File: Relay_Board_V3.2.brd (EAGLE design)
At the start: 140 x 100 mm, 59 parts

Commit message: Board Complete for 2017
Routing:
- net MOTOR_POS: track 0.00 -> 6.09 mm, vias 0 -> 1
- net MOTOR_C_SENSOR: track 23.1 -> 28.6 mm, vias 1 -> 2
- net CAP_SENSOR: track 42.9 -> 47.0 mm, vias 1 -> 2
- net FC_POS: track 52.0 -> 55.1 mm, vias 1 -> 2
- net FC.12: track 119.5 -> 120.5 mm
- net ISO_GND: track 250.2 -> 250.9 mm
- net N$3: track 59.0 -> 59.7 mm

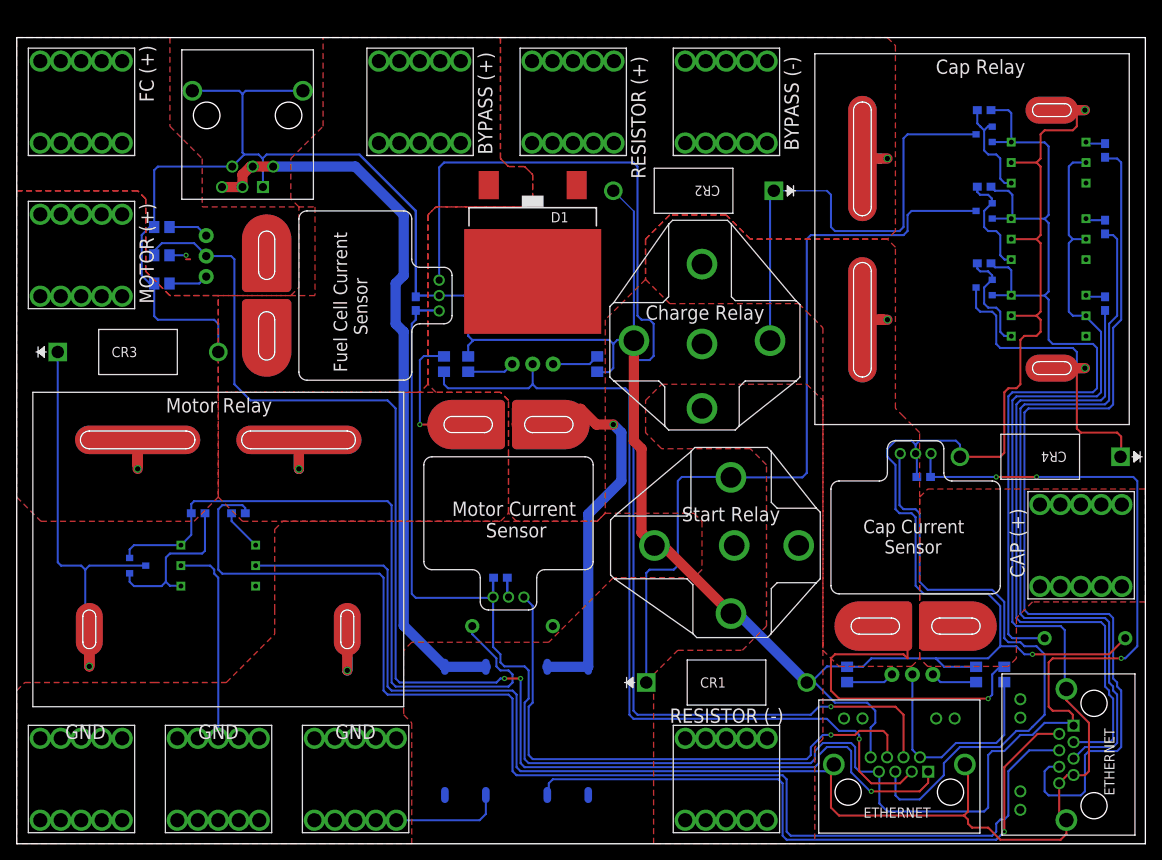
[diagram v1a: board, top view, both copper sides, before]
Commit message: Updated OptoIsolator Part so it is same as FCC
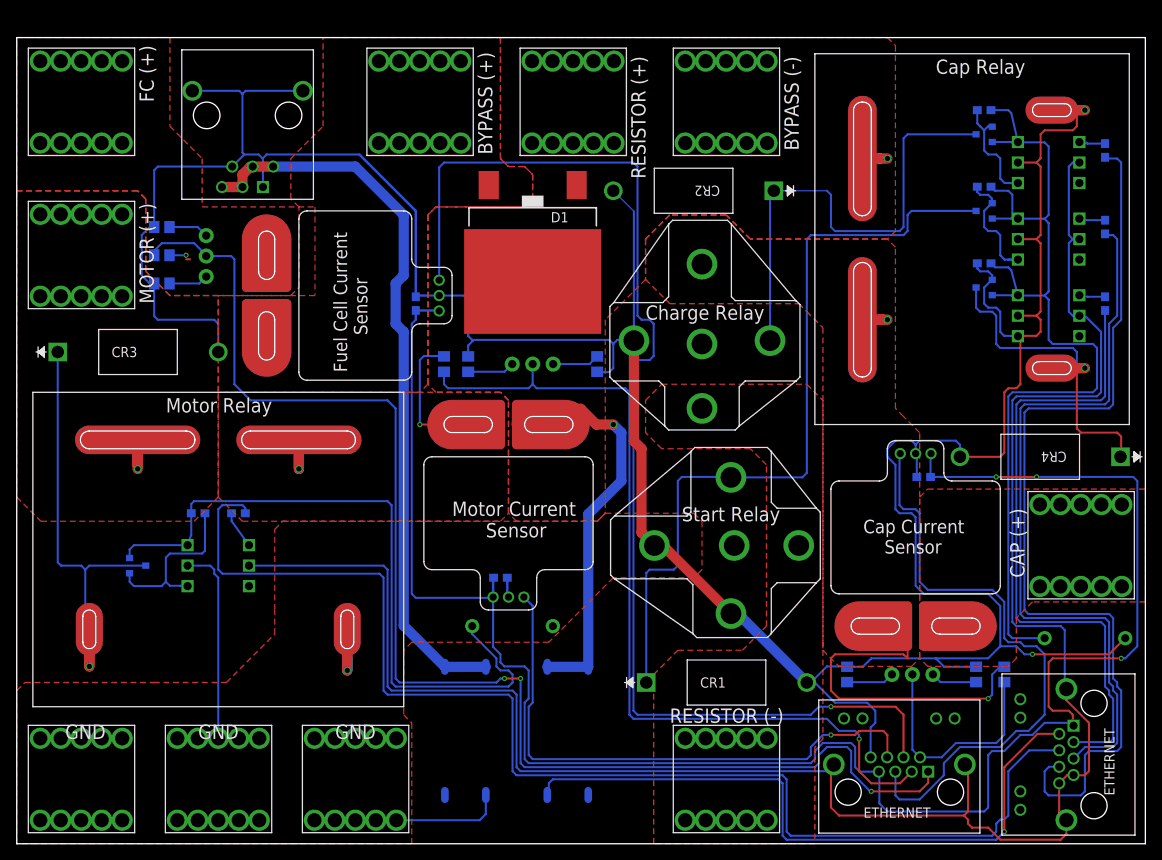
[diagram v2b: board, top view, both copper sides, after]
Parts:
- R14, R15, R16, R2, R4, R5, R6, R7, R8: device Resistor:R0805 -> resistor:R0805
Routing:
- net FC.12: track 120.5 -> 125.2 mm
- net GND: track 447.1 -> 443.8 mm
- net N$21: track 13.7 -> 15.3 mm
- net N$2: track 2.50 -> 4.07 mm
- net ISO_GND: track 250.9 -> 250.0 mm
- net N$1: track 13.2 -> 14.0 mm
- net N$4: track 20.9 -> 21.7 mm
- net N$7: track 13.5 -> 14.3 mm
- net N$8: track 2.44 -> 3.21 mm
- net N$23: track 2.44 -> 3.21 mm
- net N$5: track 5.20 -> 4.66 mm

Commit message: Added Labels to Ethernet connectors
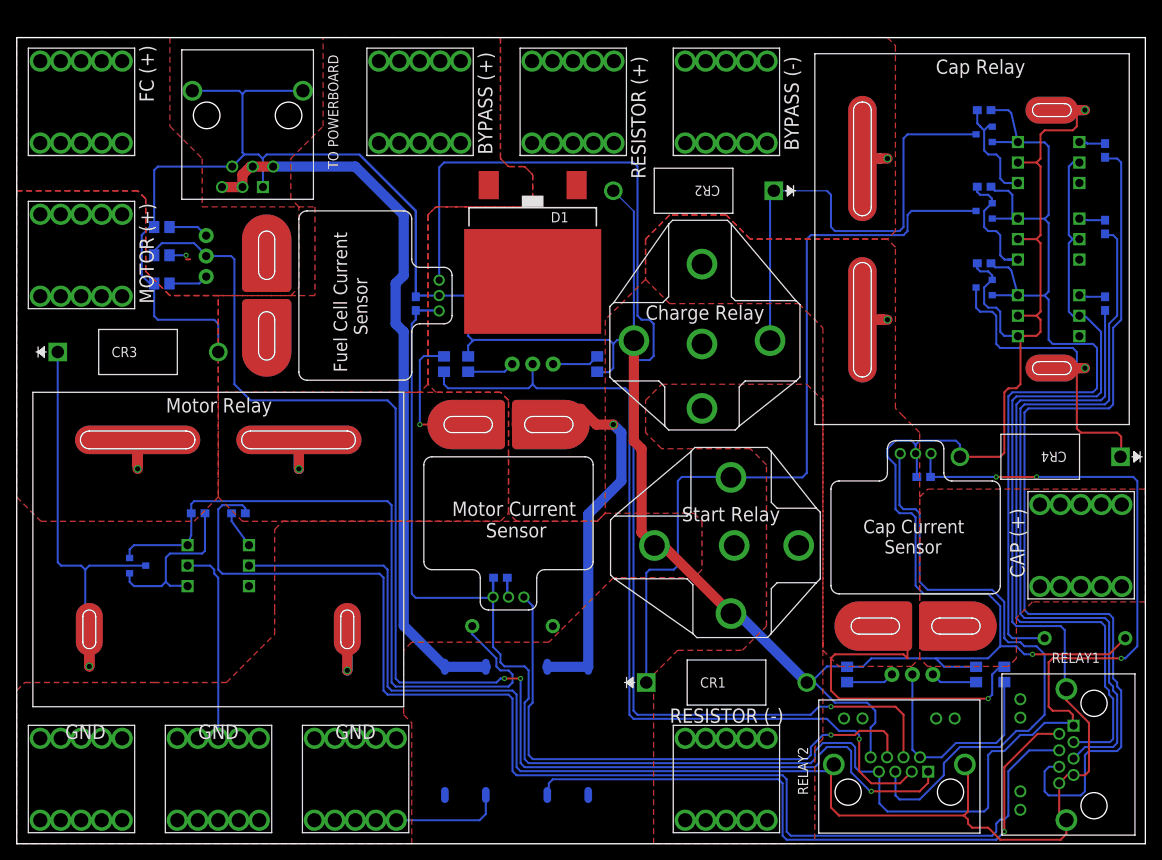
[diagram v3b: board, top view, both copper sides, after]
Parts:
- U$19: value 5555140-6 -> TO POWERBOARD
- renumbered FCC_1 to RELAY1, FCC_2 to RELAY2
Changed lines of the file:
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@@
 </autorouter>
 <elements>
-<element name="FCC_1" library="ETHERNET-3" package="A122645-ND" value="ETHERNET" x="133.630875" y="11.070175" smashed="yes" rot="R90">
-<attribute name="VALUE" x="136.170875" y="5.990175" size="1.27" layer="21" rot="R90"/>
-</element>
-<element name="FCC_2" library="ETHERNET-3" package="A122645-ND" value="ETHERNET" x="109.47946875" y="6.40385" smashed="yes">
-<attribute name="VALUE" x="105.03446875" y="3.22885" size="1.27" layer="21"/>
+<element name="RELAY1" library="ETHERNET-3" package="A122645-ND" value="ETHERNET" x="133.630875" y="11.070175" smashed="yes" rot="R90">
+<attribute name="NAME" x="134.359825" y="23.700875" size="1.27" layer="21" rot="R180"/>
+</element>
+<element name="RELAY2" library="ETHERNET-3" package="A122645-ND" value="ETHERNET" x="109.47946875" y="6.40385" smashed="yes">
+<attribute name="NAME" x="98.16615" y="6.04946875" size="1.27" layer="21" rot="R90"/>
 </element>
 <element name="R4" library="resistor" library_urn="urn:adsk.eagle:library:348" package="R0805" package3d_urn="urn:adsk.eagle:package:26059/1" value="775 (0.1%)" x="103" y="21" smashed="yes" rot="MR90">
@@
 <element name="MOTOR.GROUND" library="Connector 732-3204" package="732-3204-ND" value="732-3204-ND_CONNECTOR" x="25" y="8"/>
 <element name="CAP.GND" library="Connector 732-3204" package="732-3204-ND" value="732-3204-ND_CONNECTOR" x="8" y="8"/>
-<element name="U$19" library="5555140-6 RJ11" package="1734723-1_RJ11" value="5555140-6" x="28" y="84" smashed="yes" rot="R180"/>
+<element name="U$19" library="5555140-6 RJ11" package="1734723-1_RJ11" value="TO POWERBOARD" x="28" y="84" smashed="yes" rot="R180">
+<attribute name="VALUE" x="38.62" y="97.89" size="1.27" layer="21" rot="R270"/>
+</element>
 <element name="START.RELAY1" library="VCF4-1000" package="VCF4-1000" value="VCF4-1000" x="97" y="37"/>
 <element name="U$11" library="DMP3056L-7" package="DMP3056L-7" value="DMP3056L-7DMP3056L-7" x="120" y="78.5" rot="MR270"/>
@@
 <contactref element="U$8" pad="PIN1"/>
 <contactref element="C2" pad="1"/>
-<contactref element="FCC_1" pad="P$1"/>
-<contactref element="FCC_2" pad="P$7"/>
+<contactref element="RELAY1" pad="P$1"/>
+<contactref element="RELAY2" pad="P$7"/>
 <wire x1="59.095" y1="30.595" x2="59.09" y2="30.6" width="0.254" layer="16"/>
 <wire x1="63.5" y1="18" x2="63" y2="17.5" width="0.254" layer="16"/>
@@
 <signal name="START_R">
 <contactref element="R18" pad="2"/>
-<contactref element="FCC_1" pad="P$5"/>
+<contactref element="RELAY1" pad="P$5"/>
 <wire x1="135" y1="75.65" x2="135.15" y2="75.5" width="0.254" layer="16"/>
 <wire x1="135.15" y1="75.5" x2="136" y2="75.5" width="0.254" layer="16"/>
@@
 <signal name="MOTOR_R">
 <contactref element="R10" pad="2"/>
-<contactref element="FCC_1" pad="P$4"/>
+<contactref element="RELAY1" pad="P$4"/>
 <wire x1="28.35" y1="41" x2="28.35" y2="41.65" width="0.254" layer="16"/>
 <wire x1="28.35" y1="41.65" x2="28" y2="42" width="0.254" layer="16"/>
@@
 <signal name="CAP_R">
 <contactref element="R12" pad="2"/>
-<contactref element="FCC_1" pad="P$3"/>
+<contactref element="RELAY1" pad="P$3"/>
 <wire x1="124.5" y1="55" x2="124" y2="54.5" width="0.254" layer="16"/>
 <wire x1="124" y1="28" x2="124.5" y2="27.5" width="0.254" layer="16"/>
@@
 <signal name="CHARGE_R">
 <contactref element="R3" pad="2"/>
-<contactref element="FCC_1" pad="P$6"/>
+<contactref element="RELAY1" pad="P$6"/>
 <wire x1="135" y1="85.15" x2="135.15" y2="85" width="0.254" layer="16"/>
 <wire x1="135.15" y1="85" x2="136.5" y2="85" width="0.254" layer="16"/>
@@
 <contactref element="C2" pad="2"/>
 <contactref element="U$19" pad="1"/>
-<contactref element="FCC_2" pad="P$8"/>
+<contactref element="RELAY2" pad="P$8"/>
 <contactref element="U$14" pad="(-)"/>
 <contactref element="U$13" pad="(-)"/>
@@
 <signal name="FC_CURR">
 <contactref element="U$7" pad="PIN3"/>
-<contactref element="FCC_2" pad="P$4"/>
+<contactref element="RELAY2" pad="P$4"/>
 <wire x1="98.5" y1="16" x2="99.5" y2="17" width="0.254" layer="16"/>
 <wire x1="99.5" y1="17" x2="101" y2="17" width="0.254" layer="16"/>
@@
 <signal name="FC_VOLT">
 <contactref element="R6" pad="2"/>
-<contactref element="FCC_2" pad="P$1"/>
+<contactref element="RELAY2" pad="P$1"/>
 <contactref element="S2" pad="2"/>
 <wire x1="17.05" y1="73" x2="17.05" y2="73.55" width="0.254" layer="16"/>
@@
 <signal name="FCC_R">
 <contactref element="U$22" pad="LED+"/>
-<contactref element="FCC_1" pad="P$2"/>
+<contactref element="RELAY1" pad="P$2"/>
 <wire x1="95" y1="1" x2="95.5" y2="0.5" width="0.254" layer="16"/>
 <wire x1="95.5" y1="0.5" x2="121.5" y2="0.5" width="0.254" layer="16"/>
@@
 <signal name="CAP_CURR">
 <contactref element="U$8" pad="PIN3"/>
-<contactref element="FCC_2" pad="P$5"/>
+<contactref element="RELAY2" pad="P$5"/>
 <wire x1="108.97946875" y1="8.94385" x2="109" y2="8.92331875" width="0.254" layer="16"/>
 <wire x1="109" y1="8.92331875" x2="109" y2="6" width="0.254" layer="16"/>
@@
 <contactref element="U$4" pad="CATHODE"/>
 <contactref element="U$6" pad="CATHODE"/>
-<contactref element="FCC_1" pad="P$7"/>
-<contactref element="FCC_1" pad="P$8"/>
-<contactref element="FCC_2" pad="P$13"/>
-<contactref element="FCC_2" pad="P$14"/>
-<contactref element="FCC_1" pad="P$13"/>
-<contactref element="FCC_1" pad="P$14"/>
+<contactref element="RELAY1" pad="P$7"/>
+<contactref element="RELAY1" pad="P$8"/>
+<contactref element="RELAY2" pad="P$13"/>
+<contactref element="RELAY2" pad="P$14"/>
+<contactref element="RELAY1" pad="P$13"/>
+<contactref element="RELAY1" pad="P$14"/>
 <wire x1="28.81" y1="34.5" x2="45.5" y2="34.5" width="0.254" layer="16"/>
 <wire x1="45.5" y1="34.5" x2="46" y2="34" width="0.254" layer="16"/>
@@
 <signal name="MOTOR_CURR">
 <contactref element="U$9" pad="PIN3"/>
-<contactref element="FCC_2" pad="P$6"/>
+<contactref element="RELAY2" pad="P$6"/>
 <wire x1="62.91" y1="30.6" x2="64" y2="29.51" width="0.254" layer="16"/>
 <wire x1="64" y1="29.51" x2="64" y2="17.5" width="0.254" layer="16"/>
@@
 </signal>
 <signal name="CAP_VOLT">
-<contactref element="FCC_2" pad="P$2"/>
+<contactref element="RELAY2" pad="P$2"/>
 <contactref element="R5" pad="2"/>
 <contactref element="S1" pad="2"/>
@@
 </signal>
 <signal name="MOTOR_VOLT">
-<contactref element="FCC_2" pad="P$3"/>
+<contactref element="RELAY2" pad="P$3"/>
 <contactref element="R8" pad="2"/>
 <contactref element="S3" pad="2"/>
